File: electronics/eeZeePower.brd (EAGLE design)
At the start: 25.9 x 12.7 mm, 11 parts

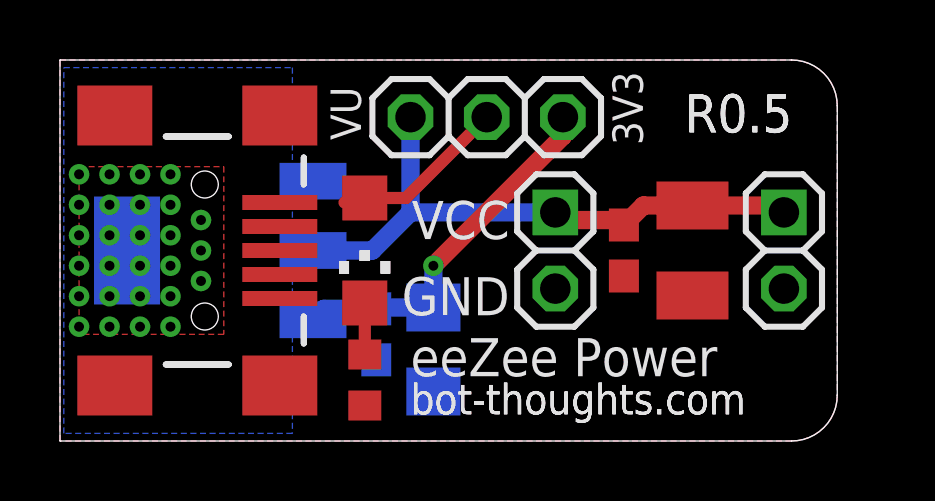
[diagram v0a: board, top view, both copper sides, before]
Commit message: minib: replaced logo; moved power select headers, passives; added help url; updated gerbers, zip
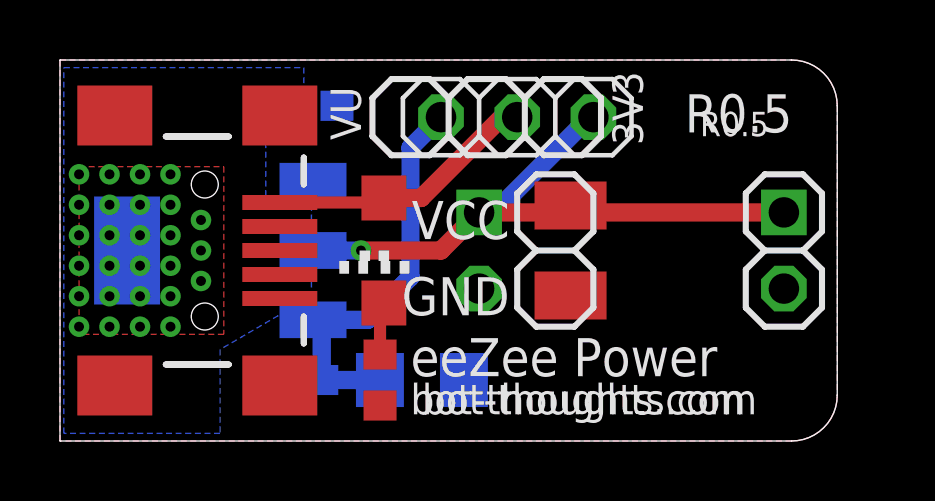
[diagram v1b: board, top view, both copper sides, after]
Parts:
- added U$2: BTLOGO-LOGO-MD, bt:BTLOGOM
- moved C3 11.5 mm to (8.38, 11.2), flipped to the bottom, turned to 180 degrees
- moved C4 4.06 mm to (17.0, 6.35)
- moved C2 3.07 mm to (7.87, 2.03), turned to 0 degrees
- moved JP3 2.54 mm to (14.0, 6.35), flipped to the bottom
- moved C1 1.09 mm to (12.1, 2.03), turned to 180 degrees
- moved JP10 1.02 mm to (15.2, 10.8), turned to 0 degrees
- moved LED1 0.63 mm to (10.8, 6.35)
- moved R1 0.51 mm to (10.7, 2.03)
- flipped JP4 to the bottom
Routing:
- net VBUS: track 5.87 -> 9.09 mm
- net VOUT: track 20.0 -> 22.4 mm, vias 27 -> 28
- net VIN: track 12.3 -> 13.7 mm, vias 1 -> 0
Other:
- board text added: "CC-BY-SA"
- board text added: "is.gd/MTPmIU"
